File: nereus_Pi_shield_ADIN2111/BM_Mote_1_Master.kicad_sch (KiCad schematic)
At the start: 29 parts, among them J1 Raspberry_Pi_2_3

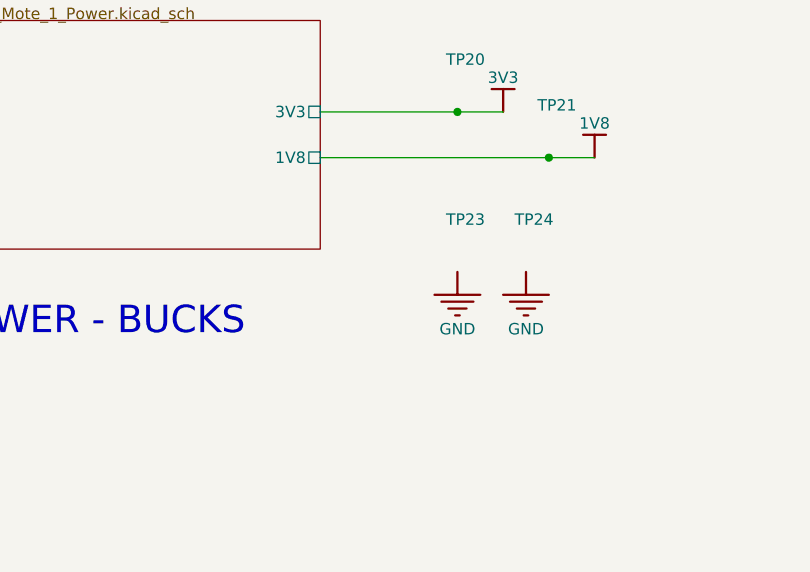
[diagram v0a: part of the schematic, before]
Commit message: S4.a: 5 V converter for the Pi (U10, copy of U5); close S3
Power sheet: U5 block copied with schedit.copy_block (new refs U10, L6,
C53-C58, R37-R40); R38 13.7k (5 V), C56/C57 22uF 16V 0805 + C58 4.7uF
10V 0402; L6 same PA5432.822NLT. Top-Level: 5V_PI sheet pin, TP38, label;
TP23/TP24 moved down to clear it. DESIGN D13. ERC 78/629, netcheck 53/53,
existing parts' connections identical.

Co-Authored-By: Claude Opus 5.5 <noreply@anthropic.com>
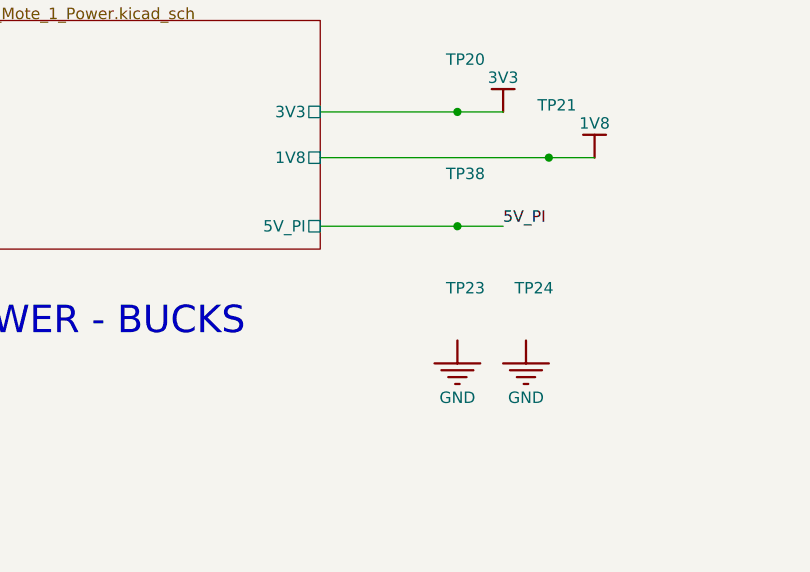
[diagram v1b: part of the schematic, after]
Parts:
- added TP38: TEST_POINT, PCB_TP_1.5mm, symbol BM_Mote_000639-AB-altium-import:Designator_3_TEST_POINT_Sofar Ocean Technologie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
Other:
- sheet Power Regulators ports: added 5V_PI; removed none

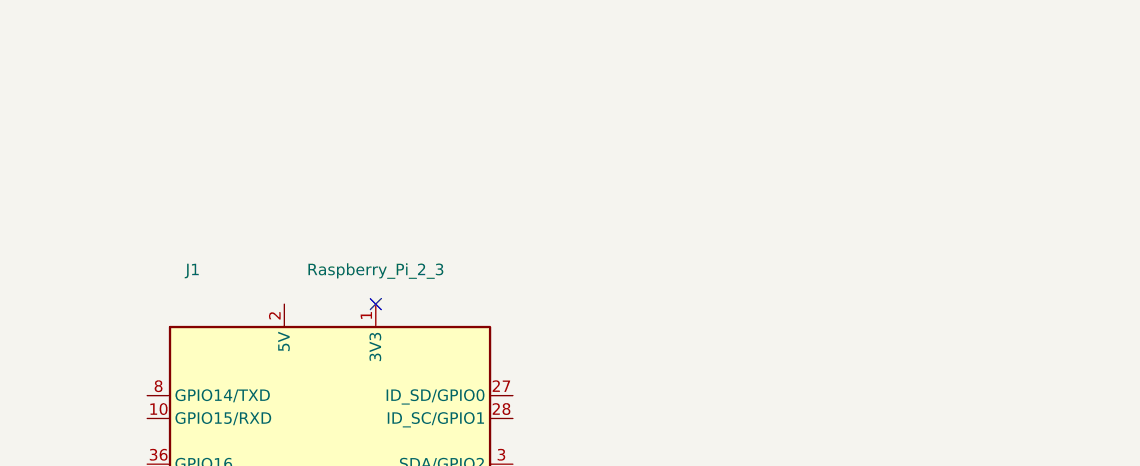
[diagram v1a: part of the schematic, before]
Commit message: S4.b: shield powers the Pi through bridged link JP1 (D14); close S4.a
Top-Level: JP1 (stock SolderJumper_2_Bridged, not in BOM) joins 5V_PI to
new net PI_5V (J1 pins 2/4); #FLG03; note. New project footprint
nereus:R_1210_Bridged_NetTie (R11's 1210 pads + 1 mm copper net tie) in
nereus.pretty with a project fp-lib-table. midwire.lib_pins fix: symbols
named like Raspberry_Pi_2_3 were skipped (+ test). ERC 76/629 (-2, J1 pin
2), netcheck 53/53, existing connections identical.

Co-Authored-By: Claude Opus 5.5 <noreply@anthropic.com>
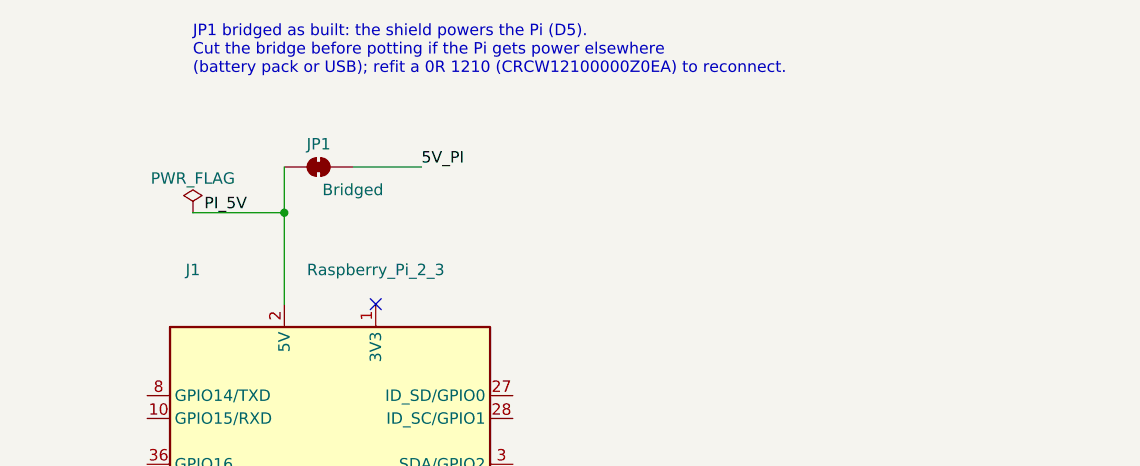
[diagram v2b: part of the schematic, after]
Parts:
- added JP1: Bridged, nereus:R_1210_Bridged_NetTie, symbol Jumper:SolderJumper_2_Bridged
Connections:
- net 5V_PI: now also JP1.2 (B)
- net PI_5V: now reaches J1.2 (5V), J1.4 (5V)
- net PI_5V: now also JP1.1 (A)
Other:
- note added: "JP1 bridged as built: the shield powers the Pi (D5). Cut the bridge before potting if the Pi gets power elsewhere (battery pack or USB); refit a 0R 1210 (CRCW12100000Z0EA) to reconnect."
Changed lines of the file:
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@@
 		)
 	)
+	(text "JP1 bridged as built: the shield powers the Pi (D5).\nCut the bridge before potting if the Pi gets power elsewhere\n(battery pack or USB); refit a 0R 1210 (CRCW12100000Z0EA) to reconnect."
+		(exclude_from_sim no)
+		(at 106.68 30.48 0)
+		(effects
+			(font
+				(size 1.27 1.27)
+			)
+			(justify left bottom)
+		)
+	)
 	(text_box "Processor + onboard logic runs off 3V3, and ADIN AVDD off 1V8."
 		(exclude_from_sim no)
@@
 		(color 0 0 0 0)
 	)
+	(junction
+		(at 116.84 45.72)
+		(diameter 0)
+		(color 0 0 0 0)
+	)
 	(no_connect
 		(at 127 55.88)
@@
 		)
 	)
+	(wire
+		(pts
+			(xy 116.84 55.88) (xy 116.84 45.72)
+		)
+		(stroke
+			(width 0)
+			(type default)
+		)
+	)
+	(wire
+		(pts
+			(xy 116.84 45.72) (xy 116.84 40.64)
+		)
+		(stroke
+			(width 0)
+			(type default)
+		)
+	)
+	(wire
+		(pts
+			(xy 116.84 45.72) (xy 106.68 45.72)
+		)
+		(stroke
+			(width 0)
+			(type default)
+		)
+	)
+	(wire
+		(pts
+			(xy 124.46 40.64) (xy 132.08 40.64)
+		)
+		(stroke
+			(width 0)
+			(type default)
+		)
+	)
 	(label "BM2_P"
 		(at 454.66 121.92 0)
@@
 		)
 	)
+	(label "PI_5V"
+		(at 107.95 45.72 0)
+		(effects
+			(font
+				(size 1.27 1.27)
+			)
+			(justify left bottom)
+		)
+	)
+	(label "5V_PI"
+		(at 132.08 40.64 0)
+		(effects
+			(font
+				(size 1.27 1.27)
+			)
+			(justify left bottom)
+		)
+	)
 	(symbol
 		(lib_id "BM_Mote_000639-AB-altium-import:Designator_0_Symbol_Sofar Ocean Technologies, Inc.")
@@
 				)
 			)
+		)
+	)
+	(symbol
+		(lib_id "Jumper:SolderJumper_2_Bridged")
+		(at 120.65 40.64 0)
+		(unit 1)
+		(exclude_from_sim no)
+		(in_bom no)
+		(on_board yes)
+		(dnp no)
+		(property "Reference" "JP1"
+			(at 120.65 38.1 0)
+			(effects
+				(font
+					(size 1.27 1.27)
+				)
+			)
+		)
+		(property "Value" "Bridged"
+			(at 124.46 43.18 0)
+			(effects
+				(font
+					(size 1.27 1.27)
+				)
+			)
+		)
+		(property "Footprint" "nereus:R_1210_Bridged_NetTie"
+			(at 120.65 40.64 0)
+			(effects
+				(font
+					(size 1.27 1.27)
+				)
+				(hide yes)
+			)
+		)
+		(property "Datasheet" ""
+			(at 120.65 40.64 0)
+			(effects
+				(font
+					(size 1.27 1.27)
+				)
+				(hide yes)
+			)
+		)
+		(property "Description" "Bridged 0 ohm link (net tie, 1210 pads): cut to isolate the Pi's 5 V; refit CRCW12100000Z0EA to reconnect"
+			(at 120.65 40.64 0)
+			(effects
+				(font
+					(size 1.27 1.27)
+				)
+				(hide yes)
+			)
+		)
+		(pin "1"
+		)
+		(pin "2"
+		)
+		(instances
+			(project ""
+				(path "/30e82bf5-1344-486b-817c-02d3b0649ce4/3c398828-e355-49f6-be37-cb3640d2c671"
+					(reference "JP1")
+					(unit 1)
+				)
+			)
+		)
+	)
+	(symbol
+		(lib_id "power:PWR_FLAG")
+		(at 106.68 45.72 0)
+		(unit 1)
+		(exclude_from_sim no)
+		(in_bom yes)
+		(on_board yes)
+		(dnp no)
+		(property "Reference" "#FLG03"
+			(at 106.68 43.815 0)
+			(effects
+				(font
+					(size 1.27 1.27)
+				)
+				(hide yes)
+			)
+		)
+		(property "Value" "PWR_FLAG"
+			(at 106.68 41.91 0)
+			(effects
+				(font
+					(size 1.27 1.27)
+				)
+			)
+		)
+		(property "Footprint" ""
+			(at 106.68 45.72 0)
+			(effects
+				(font
+					(size 1.27 1.27)
+				)
+				(hide yes)
+			)
+		)
+		(property "Datasheet" ""
+			(at 106.68 45.72 0)
+			(effects
+				(font
+					(size 1.27 1.27)
+				)
+				(hide yes)
+			)
+		)
+		(property "Description" ""
+			(at 106.68 45.72 0)
+			(effects
+				(font
+					(size 1.27 1.27)
+				)
+				(hide yes)
+			)
+		)
+		(pin "1"
+		)
+		(instances
+			(project ""
+				(path "/30e82bf5-1344-486b-817c-02d3b0649ce4/3c398828-e355-49f6-be37-cb3640d2c671"
+					(reference "#FLG03")
+					(unit 1)
+				)
+			)

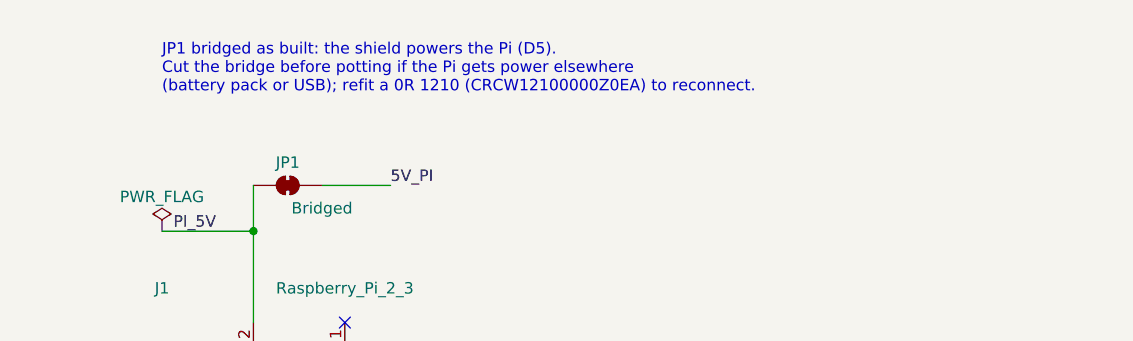
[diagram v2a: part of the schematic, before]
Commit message: S4.b: fix QE round 1 F2-F6; record F1 back-feed analysis for Nick's decision
Note cites D14 and covers any USB cable; TRACKER demo line for S4.b;
footprint renamed nereus:SolderJumper-2_R1210_Bridged_NetTie (matches the
stock symbol's filter); dead lib_pins branch removed; cut guidance. F1:
mechanism (Pi USB 5V -> L6 -> U10 HS body diode -> VBUS) in D14 and SPEC,
pending Nick's call. Report in qe/S4.md.

Co-Authored-By: Claude Opus 5.5 <noreply@anthropic.com>
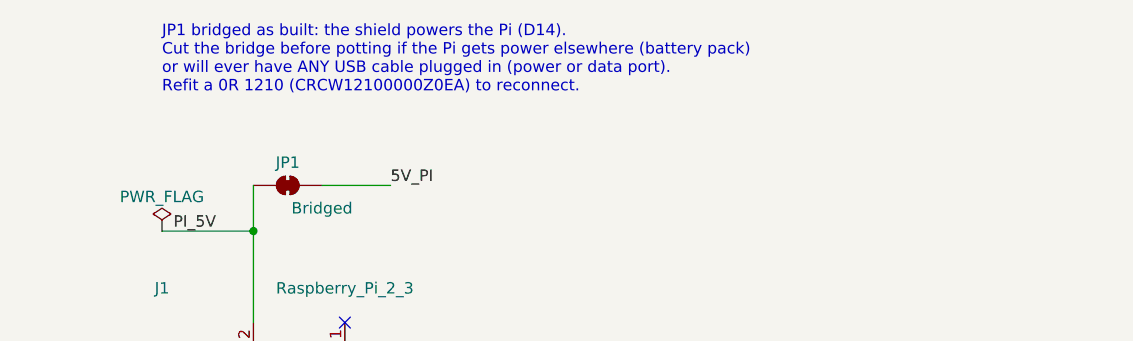
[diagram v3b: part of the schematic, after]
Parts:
- JP1: footprint nereus:R_1210_Bridged_NetTie -> nereus:SolderJumper-2_R1210_Bridged_NetTie
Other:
- note added: "JP1 bridged as built: the shield powers the Pi (D14). Cut the bridge before potting if the Pi gets power elsewhere (battery pack) or will ever have ANY USB cable plugged in (power or data port). Refit a 0R 1210 (CRCW12100000Z0EA) to reconnect."
- note removed: "JP1 bridged as built: the shield powers the Pi (D5). Cut the bridge before potting if the Pi gets power elsewhere (battery pack or USB); refit a 0R 1210 (CRCW12100000Z0EA) to reconnect."
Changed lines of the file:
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@@
 		)
 	)
-	(text "JP1 bridged as built: the shield powers the Pi (D5).\nCut the bridge before potting if the Pi gets power elsewhere\n(battery pack or USB); refit a 0R 1210 (CRCW12100000Z0EA) to reconnect."
+	(text "JP1 bridged as built: the shield powers the Pi (D14).\nCut the bridge before potting if the Pi gets power elsewhere (battery pack)\nor will ever have ANY USB cable plugged in (power or data port).\nRefit a 0R 1210 (CRCW12100000Z0EA) to reconnect."
 		(exclude_from_sim no)
 		(at 106.68 30.48 0)
@@
 			)
 		)
-		(property "Footprint" "nereus:R_1210_Bridged_NetTie"
+		(property "Footprint" "nereus:SolderJumper-2_R1210_Bridged_NetTie"
 			(at 120.65 40.64 0)
 			(effects

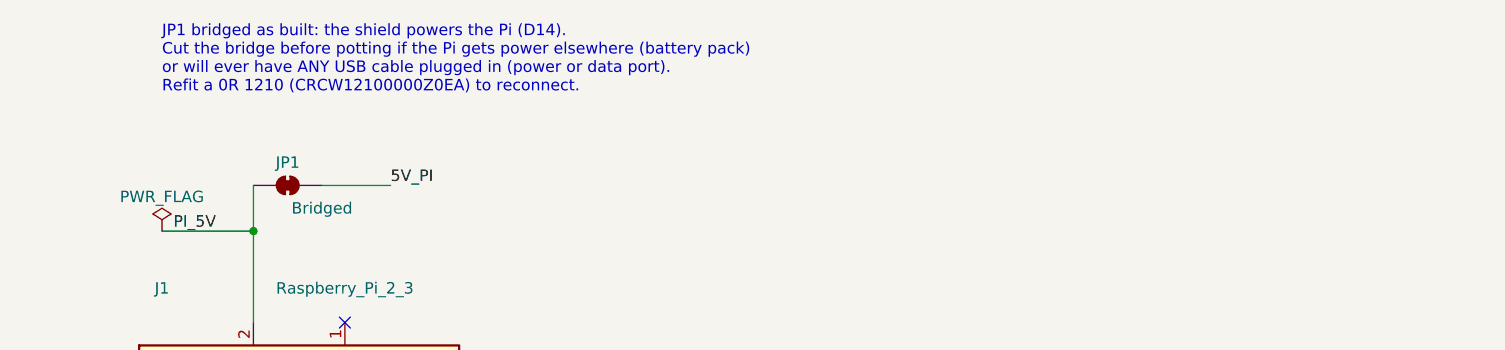
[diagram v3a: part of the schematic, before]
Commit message: S4.b: Nick keeps D14 with a bench rule (no USB 5 V source on a bridged board)
Schematic note, D14, SPEC, bench list: never plug a charger, PC host or
self-powered hub into the Pi on a bridged board, shield powered or not;
Pi-powered USB peripherals are fine and count toward the S4.c budget.

Co-Authored-By: Claude Opus 5.5 <noreply@anthropic.com>
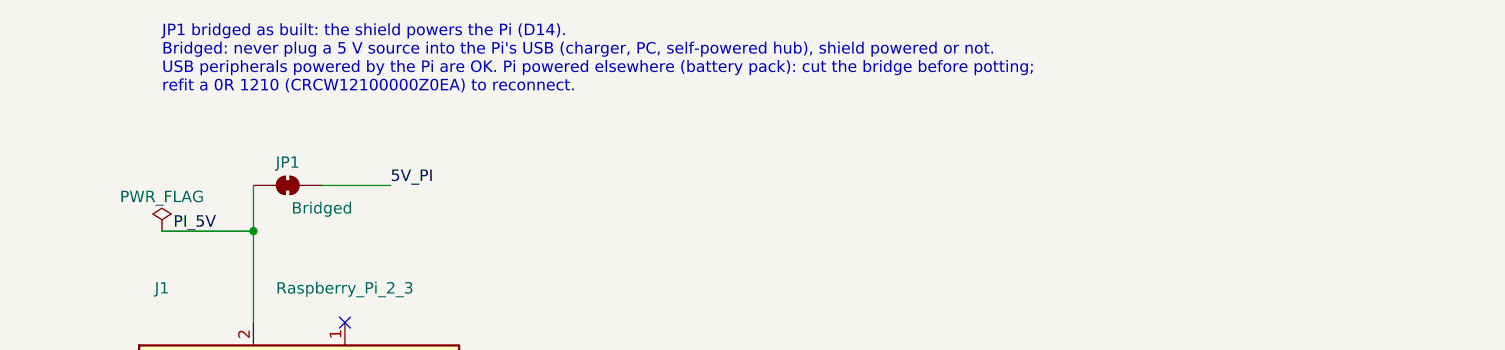
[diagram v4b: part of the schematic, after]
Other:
- note added: "JP1 bridged as built: the shield powers the Pi (D14). Bridged: never plug a 5 V source into the Pi's USB (charger, PC, self-powered hub), shield powered or not. USB peripherals powered by the Pi are OK. Pi powered elsewhere (battery pack): cut the bridge before potting; refit a 0R 1210 (CRCW12100000Z0EA) to reconnect."
- note removed: "JP1 bridged as built: the shield powers the Pi (D14). Cut the bridge before potting if the Pi gets power elsewhere (battery pack) or will ever have ANY USB cable plugged in (power or data port). Refit a 0R 1210 (CRCW12100000Z0EA) to reconnect."
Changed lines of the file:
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@@
 		)
 	)
-	(text "JP1 bridged as built: the shield powers the Pi (D14).\nCut the bridge before potting if the Pi gets power elsewhere (battery pack)\nor will ever have ANY USB cable plugged in (power or data port).\nRefit a 0R 1210 (CRCW12100000Z0EA) to reconnect."
+	(text "JP1 bridged as built: the shield powers the Pi (D14).\nBridged: never plug a 5 V source into the Pi's USB (charger, PC, self-powered hub), shield powered or not.\nUSB peripherals powered by the Pi are OK. Pi powered elsewhere (battery pack): cut the bridge before potting;\nrefit a 0R 1210 (CRCW12100000Z0EA) to reconnect."
 		(exclude_from_sim no)
 		(at 106.68 30.48 0)

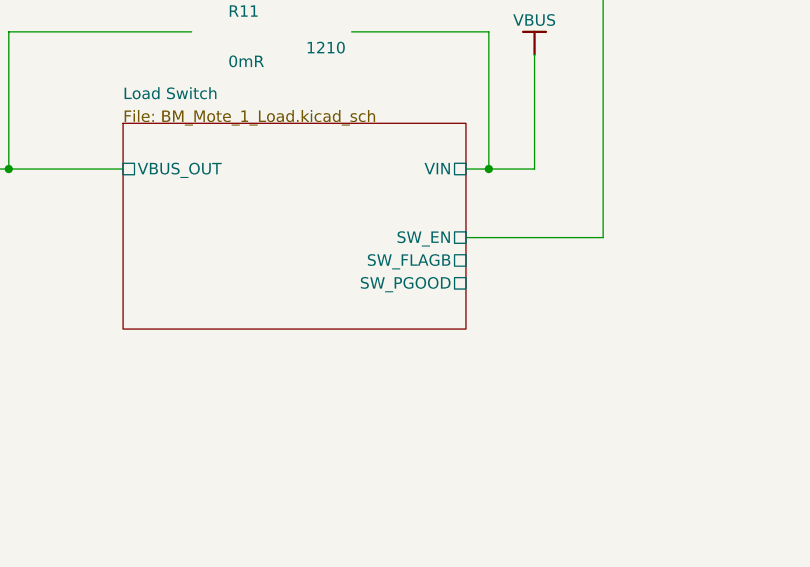
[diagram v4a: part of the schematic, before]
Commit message: S5.a: payload load switch U9 FPF2700MX (obsolete) -> U11 TPS26621DRCR; R11 DNP; Sofar brief
Load Switch sheet: U11 TI TPS26621DRCR (JLC C1848341) on new project
symbol nereus:TPS26621DRCR, stock Texas_DRC0010J footprint; R34 9.09k
(0.73 A); R41 1M IN->UVLO; dVdT NC; R32 pull-up -> R42 pull-down (SHDN
active low, payload off by default); SW_PGOOD/R33/TP34 removed. Top-Level:
R11 DNP, SW_PGOOD sheet pin removed. D18. ERC 74/626, netcheck 50/50,
kept parts identical. New docs/design-review/sofar_brief.md (mote vs
shield deviations for Sofar) + TRACKER rule.

Co-Authored-By: Claude Opus 5.5 <noreply@anthropic.com>
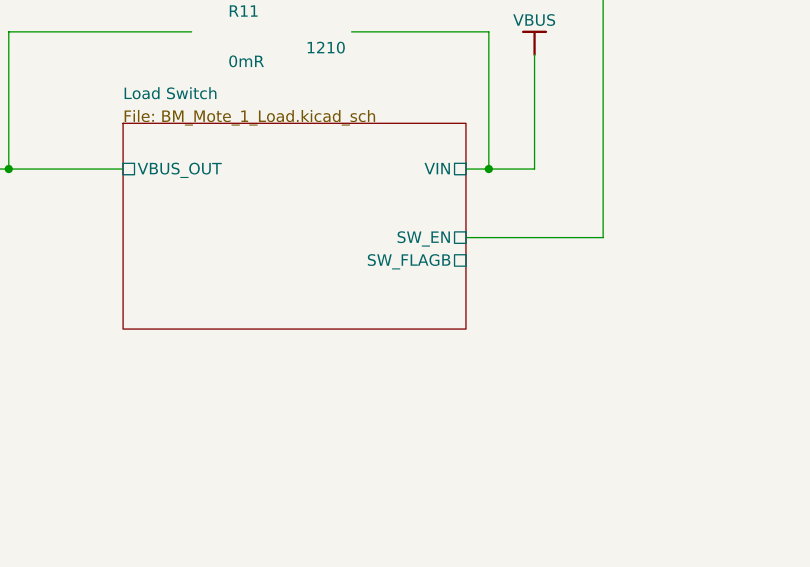
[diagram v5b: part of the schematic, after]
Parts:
- R11: now not fitted
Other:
- sheet Load Switch ports: added none; removed SW_PGOOD
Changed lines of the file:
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@@
 		(in_bom yes)
 		(on_board yes)
-		(dnp no)
+		(dnp yes)
 		(property "Reference" "R11"
 			(at 159.004 188.976 0)
@@
 			)
 		)
-		(pin "SW_PGOOD" passive
-			(at 185.42 218.44 0)
-			(effects
-				(font
-					(size 1.27 1.27)
-				)
-				(justify right)
-			)
-		)
